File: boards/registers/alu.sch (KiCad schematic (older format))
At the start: 0 parts

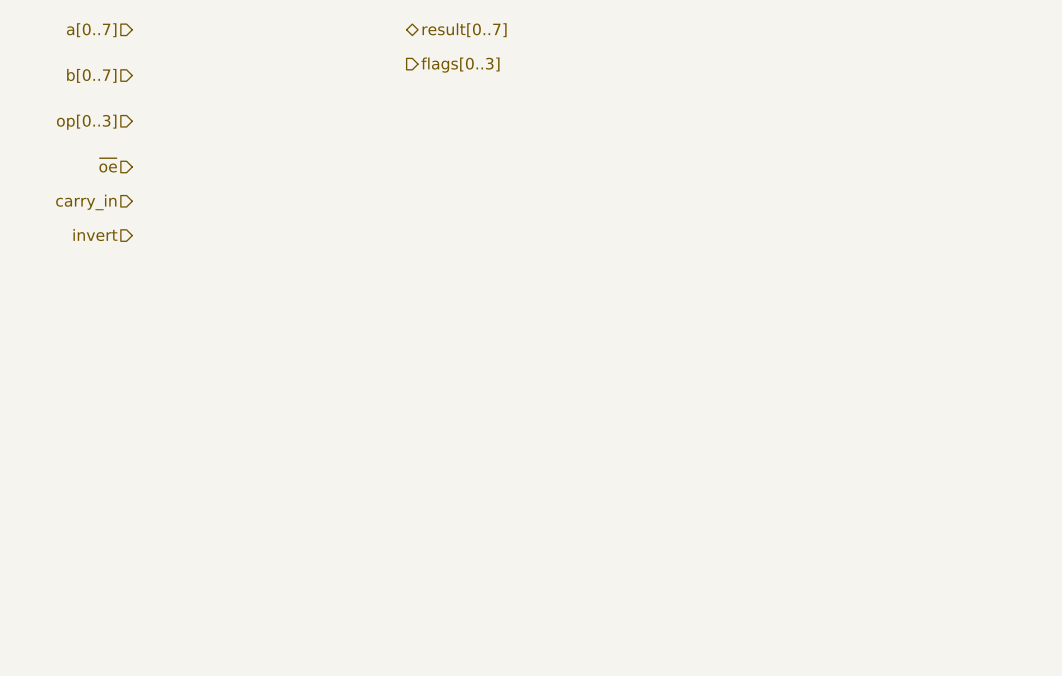
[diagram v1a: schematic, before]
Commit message: IO, ALU, and CU connectors
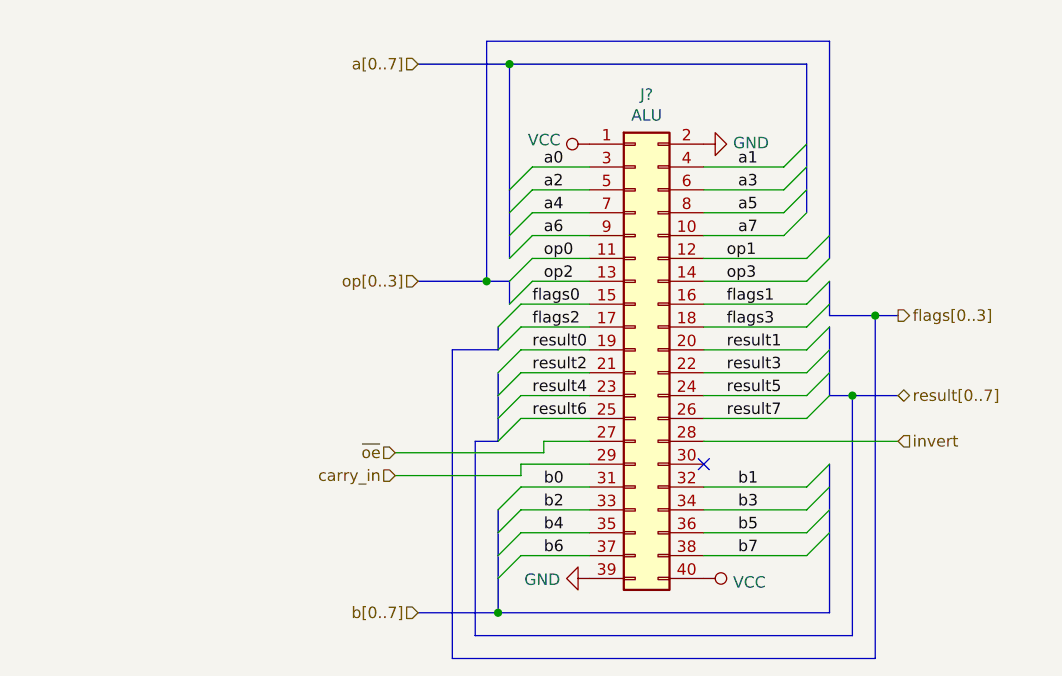
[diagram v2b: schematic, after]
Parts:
- added J?: ALU, symbol Connector_Generic:Conn_02x20_Odd_Even
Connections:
- net carry_in: now also J?.29 (Pin_29)
- net invert: now also J?.28 (Pin_28)
- net ~oe: now also J?.27 (Pin_27)
- new net GND: J?.2 (Pin_2), J?.39 (Pin_39)
- new net VCC: J?.1 (Pin_1), J?.40 (Pin_40)
- new net a0: J?.3 (Pin_3)
- new net a1: J?.4 (Pin_4)
- new net a2: J?.5 (Pin_5)
- new net a3: J?.6 (Pin_6)
- new net a4: J?.7 (Pin_7)
- new net a5: J?.8 (Pin_8)
- new net a6: J?.9 (Pin_9)
- new net a7: J?.10 (Pin_10)
- new net b0: J?.31 (Pin_31)
- new net b1: J?.32 (Pin_32)
- new net b2: J?.33 (Pin_33)
- new net b3: J?.34 (Pin_34)
- new net b4: J?.35 (Pin_35)
- new net b5: J?.36 (Pin_36)
- new net b6: J?.37 (Pin_37)
- new net b7: J?.38 (Pin_38)
- new net flags0: J?.15 (Pin_15)
- new net flags1: J?.16 (Pin_16)
- new net flags2: J?.17 (Pin_17)
- new net flags3: J?.18 (Pin_18)
- new net op0: J?.11 (Pin_11)
- new net op1: J?.12 (Pin_12)
- new net op2: J?.13 (Pin_13)
- new net op3: J?.14 (Pin_14)
- new net result0: J?.19 (Pin_19)
- new net result1: J?.20 (Pin_20)
- new net result2: J?.21 (Pin_21)
- new net result3: J?.22 (Pin_22)
- new net result4: J?.23 (Pin_23)
- new net result5: J?.24 (Pin_24)
- new net result6: J?.25 (Pin_25)
- new net result7: J?.26 (Pin_26)
- no-connect marks 0 -> 1

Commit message: Annotated schematics, assigned footprints
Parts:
- J1: renamed from J?; footprint (none) -> Connector_PinSocket_2.54mm:PinSocket_2x20_P2.54mm_Horizontal
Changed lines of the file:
@@
 flags[0..3]
 $Comp
-L Connector_Generic:Conn_02x20_Odd_Even J?
+L Connector_Generic:Conn_02x20_Odd_Even J1
 U 1 1 5ED10580
 P 4200 2700
-F 0 "J?" H 4250 3817 50  0000 C CNN
+F 0 "J1" H 4250 3817 50  0000 C CNN
 F 1 "ALU" H 4250 3726 50  0000 C CNN
-F 2 "" H 4200 2700 50  0001 C CNN
+F 2 "Connector_PinSocket_2.54mm:PinSocket_2x20_P2.54mm_Horizontal" H 4200 2700 50  0001 C CNN
 F 3 "~" H 4200 2700 50  0001 C CNN
 	1    4200 2700
@@
 $EndComp
 $Comp
-L power:GND #PWR?
+L power:GND #PWR0172
 U 1 1 5ED17F1D
 P 4500 1800
-F 0 "#PWR?" H 4500 1550 50  0001 C CNN
+F 0 "#PWR0172" H 4500 1550 50  0001 C CNN
 F 1 "GND" V 4505 1672 50  0000 R CNN
 F 2 "" H 4500 1800 50  0001 C CNN
@@
 $EndComp
 $Comp
-L power:GND #PWR?
+L power:GND #PWR0171
 U 1 1 5ED187D7
 P 4000 3700
-F 0 "#PWR?" H 4000 3450 50  0001 C CNN
+F 0 "#PWR0171" H 4000 3450 50  0001 C CNN
 F 1 "GND" V 4005 3572 50  0000 R CNN
 F 2 "" H 4000 3700 50  0001 C CNN
@@
 $EndComp
 $Comp
-L power:VCC #PWR?
+L power:VCC #PWR0170
 U 1 1 5ED1982C
 P 4000 1800
-F 0 "#PWR?" H 4000 1650 50  0001 C CNN
+F 0 "#PWR0170" H 4000 1650 50  0001 C CNN
 F 1 "VCC" V 4018 1927 50  0000 L CNN
 F 2 "" H 4000 1800 50  0001 C CNN
@@
 $EndComp
 $Comp
-L power:VCC #PWR?
+L power:VCC #PWR0173
 U 1 1 5ED1A175
 P 4500 3700
-F 0 "#PWR?" H 4500 3550 50  0001 C CNN
+F 0 "#PWR0173" H 4500 3550 50  0001 C CNN
 F 1 "VCC" V 4517 3828 50  0000 L CNN
 F 2 "" H 4500 3700 50  0001 C CNN

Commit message: PCB attempt
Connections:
- wire segments 39 -> 33
- no-connect marks 1 -> 0
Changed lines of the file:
@@
 $EndComp
 Entry Wire Line
-	3650 2000 3750 1900
+	3650 3400 3750 3300
 Entry Wire Line
-	3650 2100 3750 2000
+	3650 3500 3750 3400
 Entry Wire Line
-	3650 2200 3750 2100
+	3650 3600 3750 3500
 Entry Wire Line
-	3650 2300 3750 2200
+	3650 3700 3750 3600
 Entry Wire Line
-	3600 3400 3700 3300
+	3600 3000 3700 2900
 Entry Wire Line
-	3600 3500 3700 3400
+	3600 3100 3700 3000
 Entry Wire Line
-	3600 3600 3700 3500
+	3600 3200 3700 3100
 Entry Wire Line
-	3600 3700 3700 3600
+	3600 3300 3700 3200
 Wire Wire Line
-	3750 1900 4000 1900
+	3750 3300 4000 3300
 Wire Wire Line
-	4000 2000 3750 2000
+	4000 3400 3750 3400
 Wire Wire Line
-	3750 2100 4000 2100
+	3750 3500 4000 3500
 Wire Wire Line
-	4000 2200 3750 2200
-Entry Wire Line
-	4850 1900 4950 1800
-Entry Wire Line
-	4850 2000 4950 1900
-Entry Wire Line
-	4850 2100 4950 2000
-Entry Wire Line
-	4850 2200 4950 2100
+	4000 3600 3750 3600
 Entry Wire Line
 	4950 3300 5050 3200
@@
 Entry Wire Line
 	4950 3600 5050 3500
+Entry Wire Line
+	4950 2900 5050 2800
+Entry Wire Line
+	4950 3000 5050 2900
+Entry Wire Line
+	4950 3100 5050 3000
+Entry Wire Line
+	4950 3200 5050 3100
+Text Label 3800 3300 0    50   ~ 0
+a0
+Text Label 3800 3400 0    50   ~ 0
+a2
+Text Label 3800 3500 0    50   ~ 0
+a4
+Text Label 3800 3600 0    50   ~ 0
+a6
+Text Label 4650 3300 0    50   ~ 0
+a1
+Text Label 4650 3400 0    50   ~ 0
+a3
+Text Label 4650 3500 0    50   ~ 0
+a5
+Text Label 4650 3600 0    50   ~ 0
+a7
 Wire Wire Line
-	4500 1900 4850 1900
+	4500 2900 4950 2900
 Wire Wire Line
-	4850 2000 4500 2000
+	4500 3000 4950 3000
 Wire Wire Line
-	4500 2100 4850 2100
+	4500 3100 4950 3100
 Wire Wire Line
-	4850 2200 4500 2200
-Text Label 3800 1900 0    50   ~ 0
-a0
-Text Label 3800 2000 0    50   ~ 0
-a2
-Text Label 3800 2100 0    50   ~ 0
-a4
-Text Label 3800 2200 0    50   ~ 0
-a6
-Text Label 4650 1900 0    50   ~ 0
-a1
-Text Label 4650 2000 0    50   ~ 0
-a3
-Text Label 4650 2100 0    50   ~ 0
-a5
-Text Label 4650 2200 0    50   ~ 0
-a7
+	4500 3200 4950 3200
+Wire Wire Line
+	3700 2900 4000 2900
+Wire Wire Line
+	4000 3000 3700 3000
+Wire Wire Line
+	3700 3100 4000 3100
+Wire Wire Line
+	4000 3200 3700 3200
+Text Label 3800 2900 0    50   ~ 0
+b0
+Text Label 3800 3100 0    50   ~ 0
+b2
+Text Label 4650 2900 0    50   ~ 0
+b4
+Text Label 4650 3100 0    50   ~ 0
+b6
+Text Label 3800 3000 0    50   ~ 0
+b1
+Text Label 3800 3200 0    50   ~ 0
+b3
+Text Label 4650 3000 0    50   ~ 0
+b5
+Text Label 4650 3200 0    50   ~ 0
+b7
+Entry Wire Line
+	1850 1900 1950 1800
+Entry Wire Line
+	1850 2000 1950 1900
+Entry Wire Line
+	2800 1900 2900 1800
+Entry Wire Line
+	2800 2000 2900 1900
+Wire Wire Line
+	2800 1900 2350 1900
+Wire Wire Line
+	2350 2000 2800 2000
+Text Label 2450 1900 0    50   ~ 0
+op1
+Text Label 2450 2000 0    50   ~ 0
+op3
+Wire Wire Line
+	1950 1800 2200 1800
+Wire Wire Line
+	2200 1900 1950 1900
+Text Label 2000 1800 0    50   ~ 0
+op0
+Text Label 2000 1900 0    50   ~ 0
+op2
+Entry Wire Line
+	1800 2100 1900 2000
+Entry Wire Line
+	1800 2200 1900 2100
+Entry Wire Line
+	2800 2100 2900 2000
+Entry Wire Line
+	2800 2200 2900 2100
+Wire Wire Line
+	2800 2100 2350 2100
+Wire Wire Line
+	2350 2200 2800 2200
+Text Label 1950 2000 0    50   ~ 0
+flags0
+Text Label 1950 2100 0    50   ~ 0
+flags2
+Text Label 2450 2100 0    50   ~ 0
+flags1
+Text Label 2450 2200 0    50   ~ 0
+flags3
+Text Label 1600 3650 0    50   ~ 0
+result7
+Text Label 1600 3550 0    50   ~ 0
+result5
+Text Label 1600 3450 0    50   ~ 0
+result3
+Text Label 1600 3350 0    50   ~ 0
+result1
+Wire Wire Line
+	1500 3650 1950 3650
+Wire Wire Line
+	1950 3550 1500 3550
+Wire Wire Line
+	1500 3450 1950 3450
+Wire Wire Line
+	1950 3350 1500 3350
+Entry Wire Line
+	1950 3350 2050 3250
+Entry Wire Line
+	1950 3450 2050 3350
+Entry Wire Line
+	1950 3550 2050 3450
+Entry Wire Line
+	1950 3650 2050 3550
+Entry Wire Line
+	1800 2800 1900 2700
+Entry Wire Line
+	1800 2700 1900 2600
+Entry Wire Line
+	1800 2400 1900 2300
+Entry Wire Line
+	1800 2300 1900 2200
+Wire Wire Line
+	2200 2700 1900 2700
+Wire Wire Line
+	1900 2600 2200 2600
+Wire Wire Line
+	2200 2300 1900 2300
+Wire Wire Line
+	1900 2200 2200 2200
+Text Label 1950 2200 0    50   ~ 0
+result0
+Text Label 1950 2300 0    50   ~ 0
+result2
+Text Label 1950 2600 0    50   ~ 0
+result4
+Text Label 1950 2700 0    50   ~ 0
+result6
+Wire Wire Line
+	1900 2000 2200 2000
+Wire Wire Line
+	1900 2100 2200 2100
+Wire Wire Line
+	2350 3750 1500 3750
 Wire Wire Line
 	4500 3300 4950 3300
@@
 Wire Wire Line
 	4500 3600 4950 3600
-Wire Wire Line
-	3700 3300 4000 3300
-Wire Wire Line
-	4000 3400 3700 3400
-Wire Wire Line
-	3700 3500 4000 3500
-Wire Wire Line
-	4000 3600 3700 3600
-Text Label 3800 3300 0    50   ~ 0
-b0
-Text Label 3800 3400 0    50   ~ 0
-b2
-Text Label 3800 3500 0    50   ~ 0
-b4
-Text Label 3800 3600 0    50   ~ 0
-b6
-Text Label 4650 3300 0    50   ~ 0
-b1
-Text Label 4650 3400 0    50   ~ 0
-b3
-Text Label 4650 3500 0    50   ~ 0
-b5
-Text Label 4650 3600 0    50   ~ 0
-b7
-Entry Wire Line
-	3650 2400 3750 2300
-Entry Wire Line
-	3650 2500 3750 2400
-Entry Wire Line
-	4950 2300 5050 2200
-Entry Wire Line
-	4950 2400 5050 2300
-Wire Wire Line
-	4950 2300 4500 2300
-Wire Wire Line
-	4500 2400 4950 2400
-Text Label 4600 2300 0    50   ~ 0
-op1
-Text Label 4600 2400 0    50   ~ 0
-op3
-Wire Wire Line
-	3750 2300 4000 2300
-Wire Wire Line
-	4000 2400 3750 2400
-Text Label 3800 2300 0    50   ~ 0
-op0
-Text Label 3800 2400 0    50   ~ 0
-op2
-Entry Wire Line
-	3600 2600 3700 2500
-Entry Wire Line
-	3600 2700 3700 2600
-Entry Wire Line
-	4950 2500 5050 2400
-Entry Wire Line
-	4950 2600 5050 2500
-Wire Wire Line
-	4950 2500 4500 2500
-Wire Wire Line
-	4500 2600 4950 2600
-Text Label 3750 2500 0    50   ~ 0
-flags0
-Text Label 3750 2600 0    50   ~ 0
-flags2
-Text Label 4600 2500 0    50   ~ 0
-flags1
-Text Label 4600 2600 0    50   ~ 0
-flags3
-Text Label 4600 3000 0    50   ~ 0
-result7
-Text Label 4600 2900 0    50   ~ 0
-result5
-Text Label 4600 2800 0    50   ~ 0
-result3
-Text Label 4600 2700 0    50   ~ 0
-result1
-Wire Wire Line
-	4500 3000 4950 3000
-Wire Wire Line
-	4950 2900 4500 2900
-Wire Wire Line
-	4500 2800 4950 2800
-Wire Wire Line
-	4950 2700 4500 2700
-Entry Wire Line
-	4950 2700 5050 2600
-Entry Wire Line
-	4950 2800 5050 2700
-Entry Wire Line
-	4950 2900 5050 2800
-Entry Wire Line
-	4950 3000 5050 2900
-Entry Wire Line
-	3600 3100 3700 3000
-Entry Wire Line
-	3600 3000 3700 2900
-Entry Wire Line
-	3600 2900 3700 2800
-Entry Wire Line
-	3600 2800 3700 2700
-Wire Wire Line
-	4000 3000 3700 3000
-Wire Wire Line
-	3700 2900 4000 2900
-Wire Wire Line
-	4000 2800 3700 2800
-Wire Wire Line
-	3700 2700 4000 2700
-Text Label 3750 2700 0    50   ~ 0
-result0
-Text Label 3750 2800 0    50   ~ 0
-result2
-Text Label 3750 2900 0    50   ~ 0
-result4
-Text Label 3750 3000 0    50   ~ 0
-result6
-Wire Wire Line
-	3700 2500 4000 2500
-Wire Wire Line
-	3700 2600 4000 2600
-Wire Bus Line
-	4950 1450 3650 1450
-Wire Bus Line
-	3250 1450 3650 1450
-Connection ~ 3650 1450
-Wire Bus Line
-	3250 3850 3600 3850
-Wire Bus Line
-	5050 3850 3600 3850
-Connection ~ 3600 3850
-Wire Bus Line
-	5050 1350 3550 1350
-Wire Bus Line
-	3550 1350 3550 2400
-Wire Bus Line
-	3550 2400 3650 2400
-Wire Bus Line
-	3650 2400 3650 2500
-Wire Bus Line
-	3250 2400 3550 2400
-Connection ~ 3550 2400
-Wire Bus Line
-	3600 3100 3500 3100
-Wire Bus Line
-	3500 3100 3500 3950
-Wire Bus Line
-	3500 3950 5150 3950
-Wire Bus Line
-	5150 3950 5150 2900
-Wire Bus Line
-	5150 2900 5050 2900
-Wire Bus Line
-	5350 2900 5150 2900
-Connection ~ 5150 2900
-Wire Bus Line
-	3600 2600 3600 2700
-Wire Bus Line
-	3600 2700 3400 2700
-Wire Bus Line
-	3400 2700 3400 4050
-Wire Bus Line
-	3400 4050 5250 4050
-Wire Bus Line
-	5250 4050 5250 2550
-Wire Bus Line
-	5250 2550 5350 2550
-Wire Bus Line
-	5250 2550 5050 2550
-Connection ~ 5250 2550
-Wire Wire Line
-	3150 3150 3800 3150
-Wire Wire Line
-	3800 3150 3800 3100
-Wire Wire Line
-	3800 3100 4000 3100
-Wire Wire Line
-	3150 3250 3700 3250
-Wire Wire Line
-	3700 3250 3700 3200
-Wire Wire Line
-	3700 3200 4000 3200
-Wire Wire Line
-	5350 3100 4500 3100
-NoConn ~ 4500 3200
-Wire Bus Line
-	5050 1350 5050 2300
-Wire Bus Line
-	5050 2400 5050 2550
-Wire Bus Line
-	5050 2600 5050 2900
-Wire Bus Line
-	3600 2800 3600 3100
-Wire Bus Line
-	4950 1450 4950 2100
-Wire Bus Line
-	3650 1450 3650 2300
-Wire Bus Line
-	3600 3400 3600 3850
-Wire Bus Line
-	5050 3200 5050 3850
 $EndSCHEMATC
